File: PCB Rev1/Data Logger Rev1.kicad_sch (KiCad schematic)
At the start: 7 parts, among them J1 MICRO_SD, U1 SAM-M10Q, U2 ESP32-S3-MINI-1-N8

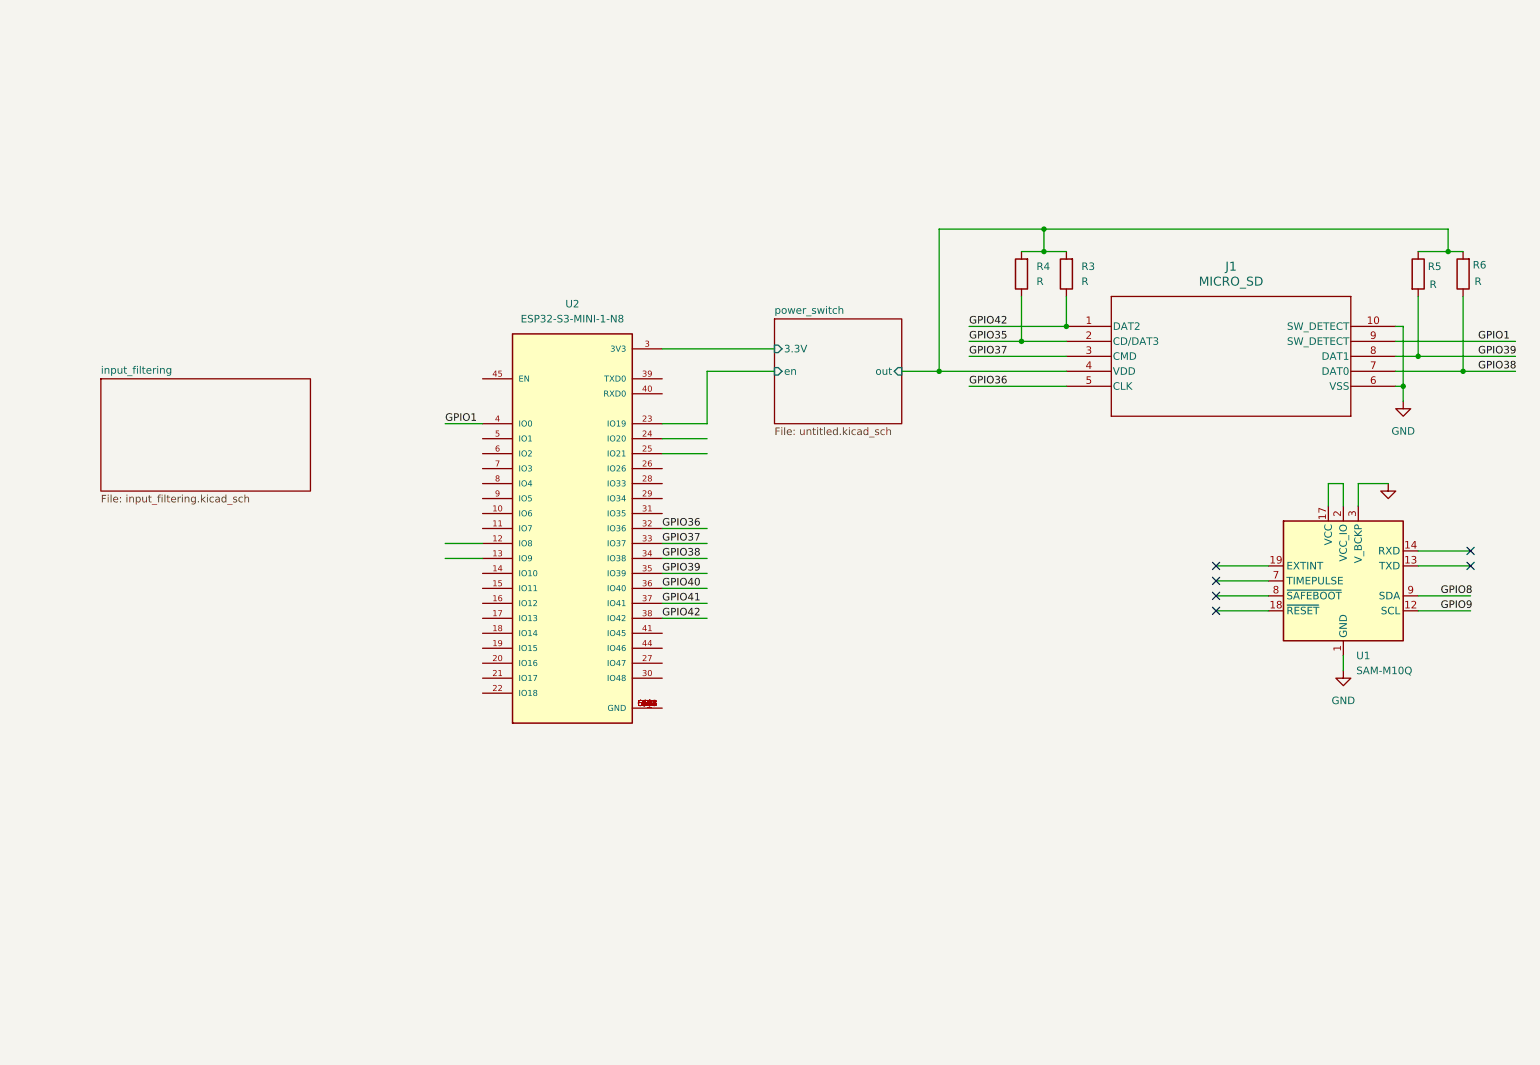
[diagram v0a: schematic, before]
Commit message: Added power filtering stage 1, DC->DC Buck
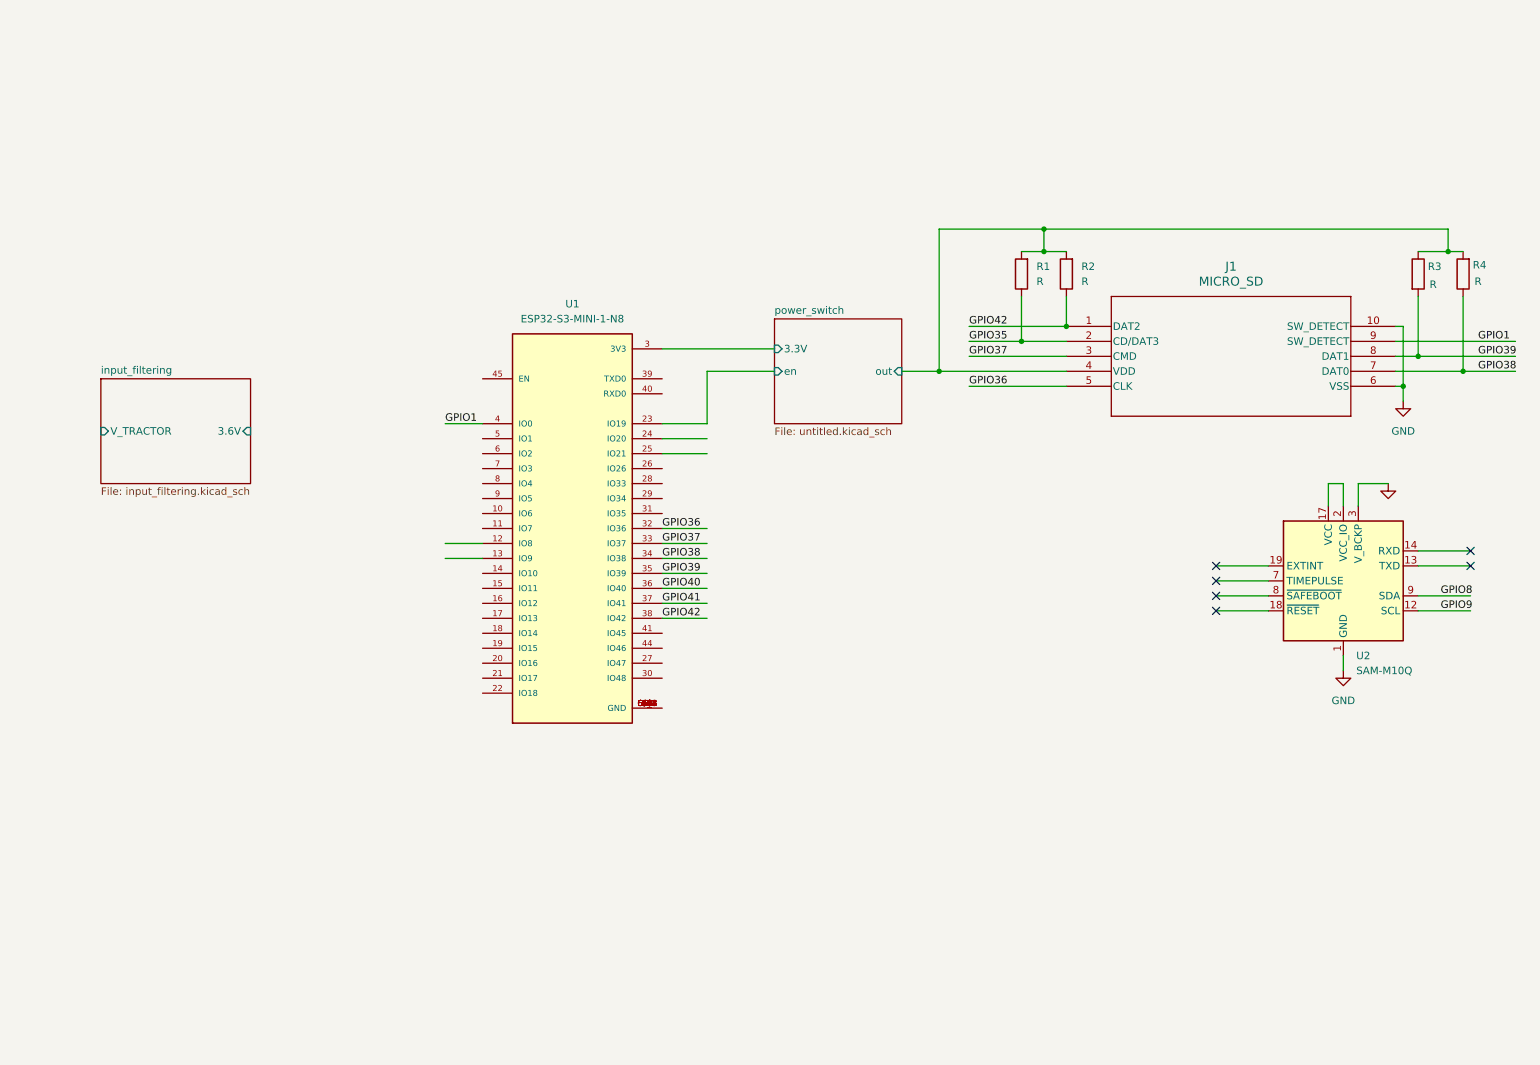
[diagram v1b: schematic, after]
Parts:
- renumbered R4 to R1, R3 to R2, R5 to R3, R6 to R4, U2 to U1, U1 to U2
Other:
- sheet input_filtering ports: added 3.6V, V_TRACTOR; removed none
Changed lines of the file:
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@@
 (kicad_sch
-	(version 20231120)
+	(version 20250114)
 	(generator "eeschema")
-	(generator_version "8.0")
+	(generator_version "9.0")
 	(paper "A4")
 	(junction
@@
 		(dnp no)
 		(fields_autoplaced yes)
-		(property "Reference" "R3"
+		(property "Reference" "R2"
 			(at 194.31 59.6899 0)
 			(effects
@@
 			(project ""
 				(path "/adf54578-0edd-4ea8-a516-35041fcd2885"
-					(reference "R3")
+					(reference "R2")
 					(unit 1)
 				)
@@
 		(dnp no)
 		(fields_autoplaced yes)
-		(property "Reference" "#PWR05"
+		(property "Reference" "#PWR01"
 			(at 238.76 134.62 0)
 			(effects
@@
 			(project "Data Logger Rev1"
 				(path "/adf54578-0edd-4ea8-a516-35041fcd2885"
-					(reference "#PWR05")
+					(reference "#PWR01")
 					(unit 1)
 				)
@@
 		(dnp no)
 		(fields_autoplaced yes)
-		(property "Reference" "R4"
+		(property "Reference" "R1"
 			(at 186.69 59.6899 0)
 			(effects
@@
 			(project "Data Logger Rev1"
 				(path "/adf54578-0edd-4ea8-a516-35041fcd2885"
-					(reference "R4")
+					(reference "R1")
 					(unit 1)
 				)
@@
 		(dnp no)
 		(fields_autoplaced yes)
-		(property "Reference" "#PWR04"
+		(property "Reference" "#PWR03"
 			(at 248.92 88.9 0)
 			(effects
@@
 			(project ""
 				(path "/adf54578-0edd-4ea8-a516-35041fcd2885"
-					(reference "#PWR04")
+					(reference "#PWR03")
 					(unit 1)
 				)
@@
 		(on_board yes)
 		(dnp no)
-		(property "Reference" "R5"
+		(property "Reference" "R3"
 			(at 254.254 59.69 0)
 			(effects
@@
 			(project "Data Logger Rev1"
 				(path "/adf54578-0edd-4ea8-a516-35041fcd2885"
-					(reference "R5")
+					(reference "R3")
 					(unit 1)
 				)
@@
 		(on_board yes)
 		(dnp no)
-		(property "Reference" "R6"
+		(property "Reference" "R4"
 			(at 261.874 59.436 0)
 			(effects
@@
 			(project "Data Logger Rev1"
 				(path "/adf54578-0edd-4ea8-a516-35041fcd2885"
-					(reference "R6")
+					(reference "R4")
 					(unit 1)
 				)
@@
 		(dnp no)
 		(fields_autoplaced yes)
-		(property "Reference" "U1"
+		(property "Reference" "U2"
 			(at 240.9541 125.73 0)
 			(effects
@@
 			(project ""
 				(path "/adf54578-0edd-4ea8-a516-35041fcd2885"
-					(reference "U1")
+					(reference "U2")
 					(unit 1)
 				)
@@
 		(dnp no)
 		(fields_autoplaced yes)
-		(property "Reference" "#PWR06"
+		(property "Reference" "#PWR02"
 			(at 246.38 102.87 0)
 			(effects
@@
 			(project "Data Logger Rev1"
 				(path "/adf54578-0edd-4ea8-a516-35041fcd2885"
-					(reference "#PWR06")
+					(reference "#PWR02")
 					(unit 1)
 				)
@@
 		(dnp no)
 		(fields_autoplaced yes)
-		(property "Reference" "U2"
+		(property "Reference" "U1"
 			(at 107.95 66.04 0)
 			(effects
@@
 			(project ""
 				(path "/adf54578-0edd-4ea8-a516-35041fcd2885"
-					(reference "U2")
+					(reference "U1")
 					(unit 1)
 				)
@@
 		(at 142.24 68.58)
 		(size 21.59 17.78)
+		(exclude_from_sim no)
+		(in_bom yes)
+		(on_board yes)
+		(dnp no)
 		(fields_autoplaced yes)
 		(stroke
@@
 	(sheet
 		(at 27.94 78.74)
-		(size 35.56 19.05)
+		(size 25.4 17.78)
+		(exclude_from_sim no)
+		(in_bom yes)
+		(on_board yes)
+		(dnp no)
 		(fields_autoplaced yes)
 		(stroke
@@
 		)
 		(property "Sheetfile" "input_filtering.kicad_sch"
-			(at 27.94 98.3746 0)
+			(at 27.94 97.1046 0)
 			(effects
 				(font
@@
 				)
 				(hide yes)
+			)
+		)
+		(pin "3.6V" input
+			(at 53.34 87.63 0)
+			(effects
+				(font
+					(size 1.27 1.27)
+				)
+				(justify right)
+			)
+		)
+		(pin "V_TRACTOR" input
+			(at 27.94 87.63 180)
+			(effects
+				(font
+					(size 1.27 1.27)
+				)
+				(justify left)
 			)
 		)
@@
 		)
 	)
+	(embedded_fonts no)
 )

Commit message: Starting work on power tree, introduced power mux
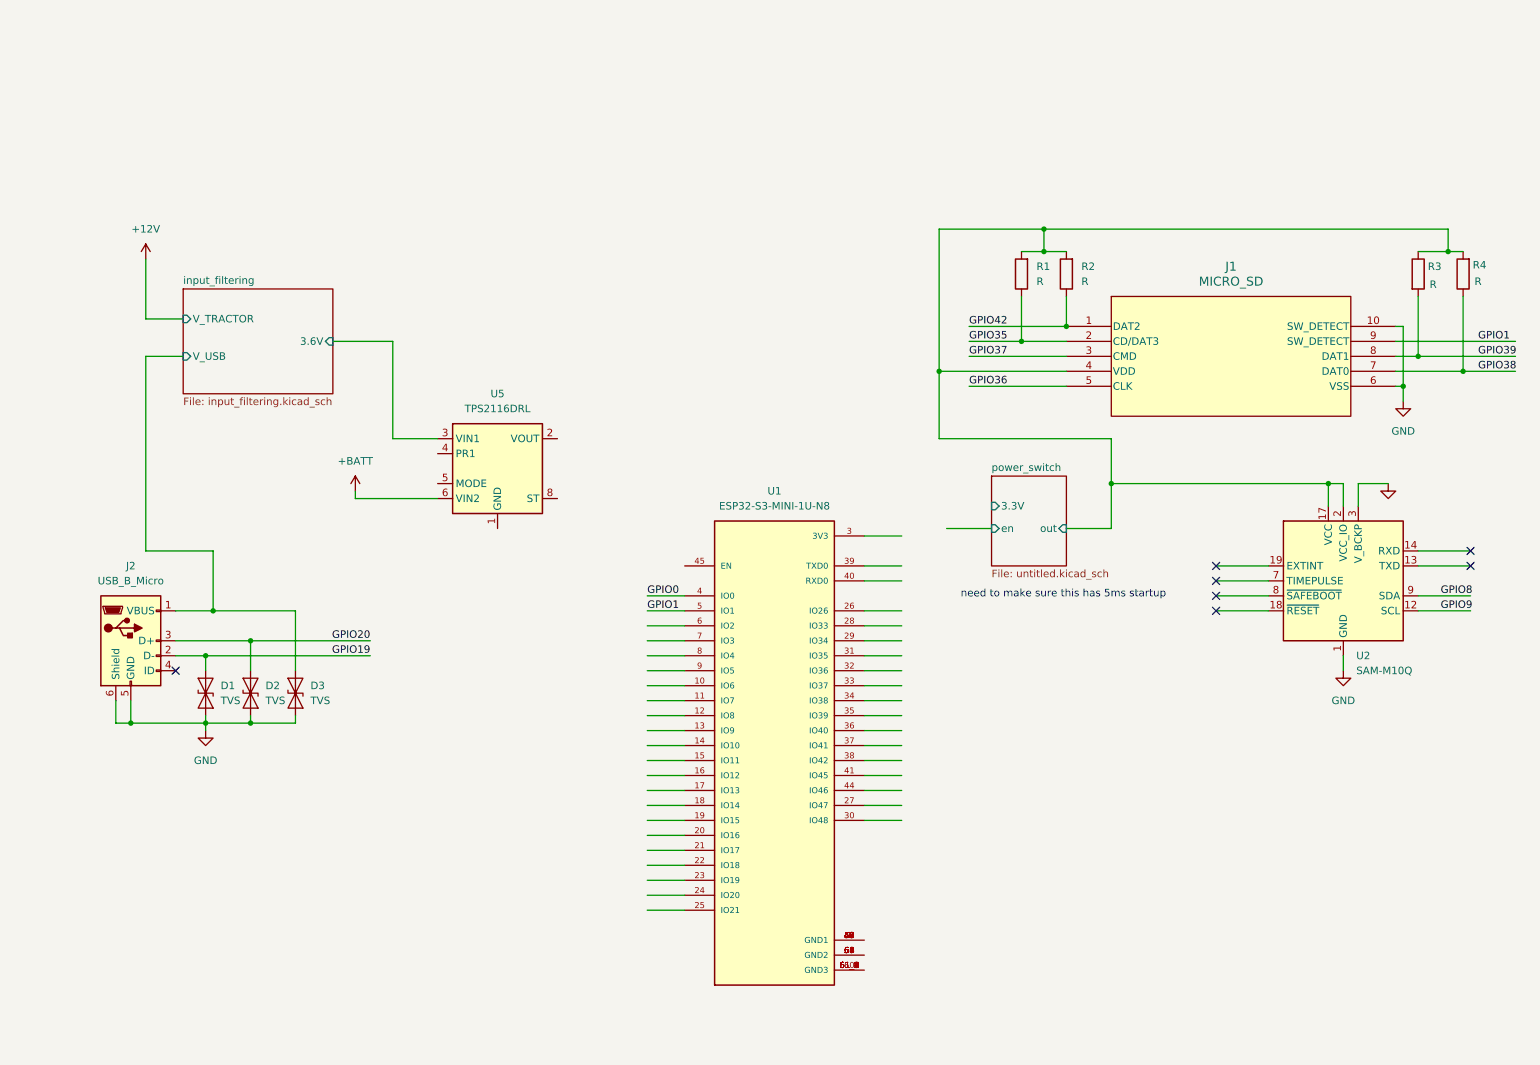
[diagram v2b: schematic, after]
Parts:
- removed U1: ESP32-S3-MINI-1-N8, ESP32-S3-MINI-1-N8:XCVR_ESP32-S3-MINI-1-N8, symbol esp32-mini:ESP32-S3-MINI-1-N8
- added D1, D2, D3: TVS, Diode_SMD:D_SMA, symbol Diode:SMAJ7.5CA
- added J2: USB_B_Micro, symbol Connector:USB_B_Micro
- added U1: ESP32-S3-MINI-1U-N8, ESP32-S3-MINI-1U-N8:XCVR_ESP32-S3-MINI-1U-N8, symbol esp32-s3-..1u:ESP32-S3-MINI-1U-N8
- added U5: TPS2116DRL, Package_TO_SOT_SMD:SOT-583-8, symbol Power_Management:TPS2116DRL
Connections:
- net GND: now also D1.1 (A1), D2.1 (A1), D3.1 (A1), J2.5 (GND), J2.6 (Shield)
- net GPIO1: now also U1.5 (IO1)
- net input_filtering/3.6V: now also U5.3 (VIN1)
- net power_switch/out: now also U2.17 (VCC), U2.2 (VCC_IO)
- new net: U5.2 (VOUT), U5.7 (VOUT)
- new net: U1.1 (GND1), U1.2 (GND1), U1.42 (GND1), U1.43 (GND1), U1.46 (GND1), U1.47 (GND1), U1.48 (GND1), U1.49 (GND1), U1.50 (GND1), U1.51 (GND1), U1.52 (GND1), U1.53 (GND1)
- new net: U1.54 (GND2), U1.55 (GND2), U1.56 (GND2), U1.57 (GND2), U1.58 (GND2), U1.59 (GND2), U1.62 (GND2), U1.63 (GND2), U1.64 (GND2), U1.65 (GND2)
- new net: U1.60 (GND3), U1.61_1 (GND3), U1.61_2 (GND3), U1.61_3 (GND3), U1.61_4 (GND3), U1.61_5 (GND3), U1.61_6 (GND3), U1.61_7 (GND3), U1.61_8 (GND3), U1.61_9 (GND3)
- new net +BATT: U5.6 (VIN2)
- new net GPIO0: U1.4 (IO0)
- new net GPIO19: D1.2 (A2), J2.2 (D-)
- new net GPIO20: D2.2 (A2), J2.3 (D+)
- new net input_filtering/V_USB: D3.2 (A2), J2.1 (VBUS)
- no-connect marks 6 -> 7
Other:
- sheet input_filtering ports: added V_USB; removed none
- note added: "need to make sure this has 5ms startup"

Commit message: Progress marches on.
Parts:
- removed U2: SAM-M10Q, RF_GPS:ublox_SAM-M8Q, symbol RF_GPS:SAM-M8Q
- added J3: Conn_01x02_Socket, Connector_PinSocket_2.54mm:PinSocket_1x02_P2.54mm_Vertical, symbol Connector:Conn_01x02_Socket
- added U2: 4492, footprints:LED_4492, symbol Neopixel:4492
- J2: footprint (none) -> Connector_USB:USB_Micro-B_Amphenol_10118193-0001LF_Horizontal
- U1: footprint ESP32-S3-MINI-1U-N8:XCVR_ESP32-S3-MINI-1U-N8 -> footprints:ESP32-S3-MINI-1U_EXP
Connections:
- net +BATT: now also J3.2 (Pin_2)
- net GND: now also J3.1 (Pin_1)
- net power_switch/3.3V: now also U1.3 (3V3)
- net input_filtering/3.6V renamed GPS Module/3.6V
- no-connect marks 7 -> 1
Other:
- added sheet GPS Module (GPS_Module.kicad_sch)
